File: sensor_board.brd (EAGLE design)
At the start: 24.9 x 49.9 mm, 9 parts, among them J1 2p-2.54, Q1 S8050

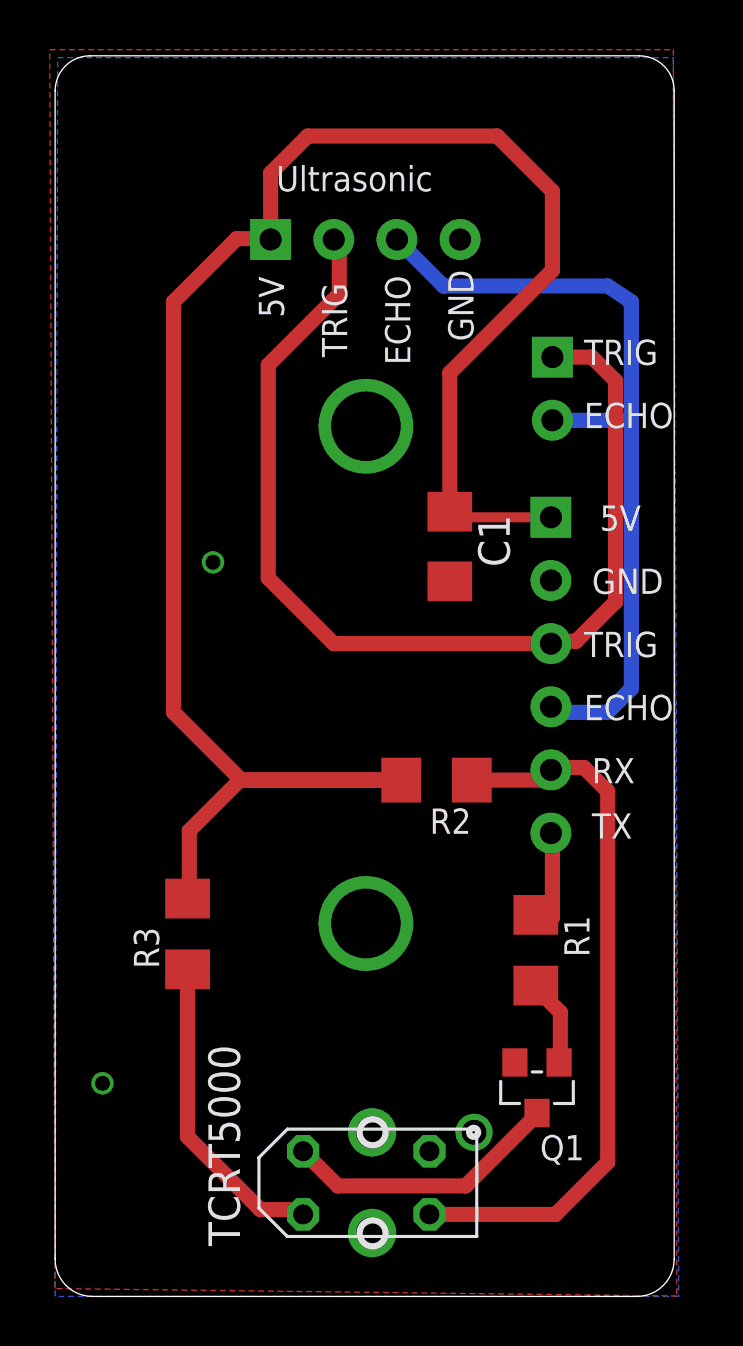
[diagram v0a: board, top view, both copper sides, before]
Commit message: PCB cosmetic changes
now, READY for sensing to SEEED for v1 fabrication.
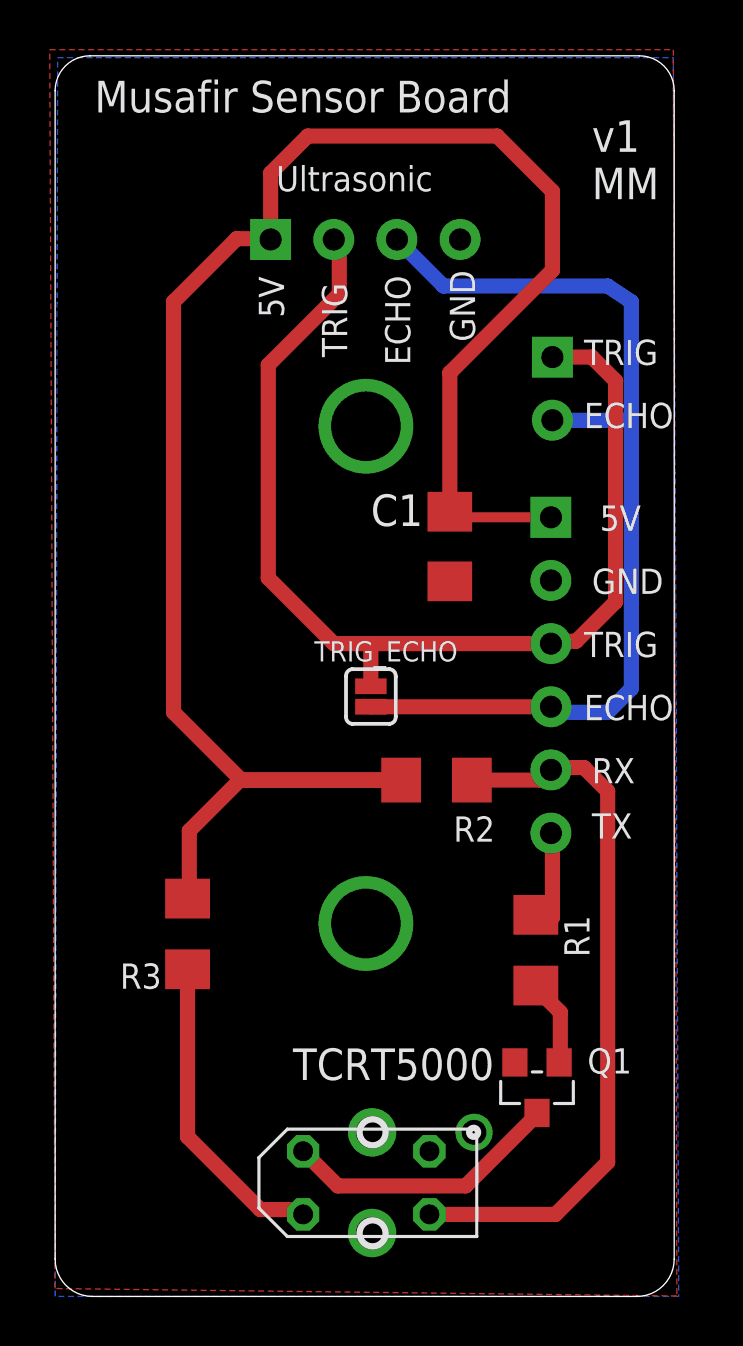
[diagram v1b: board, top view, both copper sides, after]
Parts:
- added TRIG_ECHO: (no value), SparkFun-Retired:SJ_2S
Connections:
- net ECHO: now also TRIG_ECHO.2
- net TRIG: now also TRIG_ECHO.1
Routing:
- net ECHO: track 33.5 -> 40.5 mm
- net TRIG: track 42.5 -> 44.2 mm
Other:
- board text added: "MM"
- board text added: "Musafir Sensor Board"
- board text added: "ejaadtech.com"
- board text added: "v1"
- board text removed: "EjadTech Ejadtech.com"
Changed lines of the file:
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@@
 <?xml version="1.0" encoding="utf-8"?>
 <!DOCTYPE eagle SYSTEM "eagle.dtd">
-<eagle version="7.6.0">
+<eagle version="7.2.0">
 <drawing>
 <settings>
@@
 <text x="11.7475" y="37.7825" size="1.016" layer="25" font="vector" ratio="12" rot="R90">TRIG</text>
 <text x="14.2875" y="37.465" size="1.016" layer="25" font="vector" ratio="12" rot="R90">ECHO</text>
-<text x="16.8275" y="38.4175" size="1.016" layer="25" font="vector" ratio="12" rot="R90">GND</text>
-<text x="18.415" y="30.7975" size="1.016" layer="26" font="vector" ratio="12" rot="MR0">5V</text>
-<text x="18.415" y="28.2575" size="1.016" layer="26" font="vector" ratio="12" rot="MR0">GND</text>
-<text x="18.7325" y="25.7175" size="1.016" layer="26" font="vector" ratio="12" rot="MR0">TRIG</text>
-<text x="18.615" y="23.1775" size="1.016" layer="26" font="vector" ratio="12" rot="MR0">ECHO</text>
-<text x="18.415" y="20.6375" size="1.016" layer="26" font="vector" ratio="12" rot="MR0">RX</text>
-<text x="18.415" y="18.0975" size="1.016" layer="26" font="vector" ratio="12" rot="MR0">TX</text>
+<text x="15.875" y="41.275" size="1.016" layer="25" font="vector" ratio="12" rot="R270">GND</text>
+<text x="17.78" y="30.7975" size="1.016" layer="26" font="vector" ratio="12" rot="MR0">5V</text>
+<text x="17.78" y="28.2575" size="1.016" layer="26" font="vector" ratio="12" rot="MR0">GND</text>
+<text x="18.0975" y="25.7175" size="1.016" layer="26" font="vector" ratio="12" rot="MR0">TRIG</text>
+<text x="17.98" y="23.1775" size="1.016" layer="26" font="vector" ratio="12" rot="MR0">ECHO</text>
+<text x="17.78" y="20.6375" size="1.016" layer="26" font="vector" ratio="12" rot="MR0">RX</text>
+<text x="17.78" y="18.0975" size="1.016" layer="26" font="vector" ratio="12" rot="MR0">TX</text>
 <text x="8.89" y="44.45" size="1.016" layer="25" font="vector" ratio="12">Ultrasonic</text>
-<text x="5.08" y="33.02" size="1.27" layer="26" font="vector" ratio="12" rot="MR270">EjadTech
-Ejadtech.com</text>
+<text x="5.3975" y="48.5775" size="1.27" layer="26" font="vector" ratio="12" rot="MR180">ejaadtech.com</text>
 <text x="21.2725" y="34.925" size="1.016" layer="25" font="vector" ratio="12">ECHO</text>
 <text x="21.2725" y="37.465" size="1.016" layer="25" font="vector" ratio="12">TRIG</text>
@@
 <text x="21.59" y="20.6375" size="1.016" layer="25" font="vector" ratio="12">RX</text>
 <text x="21.59" y="18.415" size="1.016" layer="25" font="vector" ratio="12">TX</text>
+<text x="1.5875" y="47.625" size="1.27" layer="25" font="vector" ratio="12" rot="SR0">Musafir Sensor Board</text>
+<text x="21.59" y="46.0375" size="1.27" layer="25" font="vector" ratio="12" rot="SR0">v1</text>
+<text x="21.59" y="44.1325" size="1.27" layer="25" font="vector" ratio="12" rot="SR0">MM</text>
 </plain>
 <attributes>
@@
 <element name="INPUT" library="Seeed-Connector -2016" package="H6-2.54" value="6p-2.54" x="19.9425" y="24.9875" smashed="yes" rot="MR0">
 <attribute name="MPN" value="F185-1106A1BSYC1" x="19.9425" y="24.9875" size="1.778" layer="28" rot="MR0" display="off"/>
-<attribute name="VALUE" x="17.4025" y="23.0825" size="0.889" layer="28" ratio="11" rot="MR90"/>
 <attribute name="NAME" x="21.53" y="24.035" size="1.016" layer="26" font="vector" ratio="12" rot="MR90"/>
 <attribute name="NAME" x="19.3075" y="22.4475" size="0.635" layer="34" ratio="10" rot="MR90"/>
@@
 <attribute name="MPN" value="F185-1104A1BSYA1" x="12.4775" y="42.5125" size="1.778" layer="28" rot="MR270" display="off"/>
 <attribute name="NAME" x="15.0175" y="44.735" size="1.016" layer="26" font="vector" ratio="12" rot="MR0"/>
-<attribute name="VALUE" x="14.3825" y="39.9725" size="0.889" layer="28" ratio="11" rot="MR0"/>
 </element>
 <element name="Q1" library="Seeed-Transistor-2016" package="SOT-23" value="S8050" x="19.3825" y="8.395" smashed="yes" rot="R180">
 <attribute name="MPN" value="S8050" x="19.3825" y="8.395" size="1.778" layer="27" rot="R180" display="off"/>
-<attribute name="NAME" x="21.2875" y="6.49" size="1.016" layer="25" font="vector" ratio="12" rot="R180"/>
-<attribute name="VALUE" x="20.6525" y="11.189" size="0.635" layer="27" ratio="10" rot="R180"/>
+<attribute name="NAME" x="23.1925" y="9.9825" size="1.016" layer="25" font="vector" ratio="12" rot="R180"/>
 </element>
 <element name="R1" library="adafruit" package="R1206" value="" x="19.335" y="13.925" smashed="yes" rot="R270">
@@
 </element>
 <element name="R2" library="adafruit" package="R1206" value="" x="15.34" y="20.7675" smashed="yes" rot="R180">
-<attribute name="NAME" x="16.737" y="19.6245" size="1.016" layer="25" font="vector" ratio="12" rot="R180"/>
+<attribute name="NAME" x="17.6895" y="19.307" size="1.016" layer="25" font="vector" ratio="12" rot="R180"/>
 <attribute name="VALUE" x="16.737" y="23.1805" size="1.27" layer="27" rot="R180"/>
 </element>
 <element name="R3" library="adafruit" package="R1206" value="" x="5.3275" y="14.58" smashed="yes" rot="R90">
-<attribute name="NAME" x="4.1845" y="13.183" size="1.016" layer="25" font="vector" ratio="12" rot="R90"/>
+<attribute name="NAME" x="4.2795" y="13.392" size="1.016" layer="25" font="vector" ratio="12" rot="R180"/>
 <attribute name="VALUE" x="7.7405" y="13.183" size="1.27" layer="27" rot="R90"/>
 </element>
 <element name="TCRT5000" library="tcrt5000" package="TCRT5000" value="" x="12.515" y="4.57" smashed="yes">
-<attribute name="NAME" x="7.435" y="2.03" size="1.27" layer="25" font="vector" ratio="12" rot="R90"/>
+<attribute name="NAME" x="17.655" y="9.975" size="1.27" layer="25" font="vector" ratio="12" rot="R180"/>
 <attribute name="VALUE" x="18.865" y="2.03" size="1.27" layer="21" rot="R90"/>
 </element>
 <element name="C1" library="adafruit" package="C1206" value="" x="15.875" y="30.1625" smashed="yes" rot="R270">
-<attribute name="NAME" x="17.018" y="31.4325" size="1.27" layer="25" rot="R270"/>
+<attribute name="NAME" x="12.7" y="30.988" size="1.27" layer="25" font="vector" ratio="12"/>
 <attribute name="VALUE" x="13.462" y="31.4325" size="1.27" layer="27" rot="R270"/>
 </element>
 <element name="J1" library="Seeed-Connector -2016" package="H2-2.54" value="2p-2.54" x="20.0025" y="36.5125" smashed="yes" rot="MR0">
 <attribute name="MPN" value="P125-1102A0BS116A1" x="20.0025" y="36.5125" size="1.778" layer="28" rot="MR0" display="off"/>
-<attribute name="VALUE" x="17.4625" y="33.9725" size="0.889" layer="28" ratio="11" rot="MR90"/>
+</element>
+<element name="TRIG_ECHO" library="SparkFun-Retired" package="SJ_2S" value="" x="12.7" y="24.13" smashed="yes" rot="R270">
+<attribute name="NAME" x="16.1898" y="26.3525" size="0.8128" layer="25" font="vector" ratio="12" rot="R180"/>
+<attribute name="VALUE" x="11.049" y="25.0798" size="0.4064" layer="27" rot="R270"/>
 </element>
 </elements>
@@
 <wire x1="11.43" y1="40.3225" x2="11.43" y2="42.29" width="0.6096" layer="1"/>
 <wire x1="11.43" y1="42.29" x2="11.2075" y2="42.5125" width="0.6096" layer="1"/>
-<wire x1="11.2075" y1="26.2575" x2="19.9425" y2="26.2575" width="0.6096" layer="1"/>
+<wire x1="11.2075" y1="26.2575" x2="12.7" y2="26.2575" width="0.6096" layer="1"/>
+<wire x1="12.7" y1="26.2575" x2="19.9425" y2="26.2575" width="0.6096" layer="1"/>
 <wire x1="20.0025" y1="37.7825" x2="21.59" y2="37.7825" width="0.6096" layer="1"/>
 <wire x1="22.5425" y1="27.94" x2="20.955" y2="26.3525" width="0.6096" layer="1"/>
@@
 <wire x1="22.5425" y1="27.94" x2="22.5425" y2="36.83" width="0.6096" layer="1"/>
 <wire x1="22.5425" y1="36.83" x2="21.59" y2="37.7825" width="0.6096" layer="1"/>
+<contactref element="TRIG_ECHO" pad="1"/>
+<wire x1="12.7" y1="24.5419" x2="12.7" y2="26.2575" width="0.6096" layer="1"/>
 </signal>
 <signal name="5V">
@@
 <contactref element="INPUT" pad="4"/>
 <contactref element="J1" pad="2"/>
-<wire x1="19.72" y1="23.495" x2="19.9425" y2="23.7175" width="0.6096" layer="1"/>
 <wire x1="13.7475" y1="42.5125" x2="13.7475" y2="42.1325" width="0.6096" layer="16"/>
 <wire x1="23.1775" y1="24.4475" x2="22.225" y2="23.495" width="0.6096" layer="16"/>
@@
 <wire x1="23.1775" y1="40.005" x2="23.1775" y2="35.2425" width="0.6096" layer="16"/>
 <wire x1="23.1775" y1="35.2425" x2="23.1775" y2="24.4475" width="0.6096" layer="16"/>
+<contactref element="TRIG_ECHO" pad="2"/>
+<wire x1="19.9425" y1="23.7175" x2="12.7" y2="23.7175" width="0.6096" layer="1"/>
+<wire x1="12.7" y1="23.7175" x2="12.7" y2="23.7181" width="0.6096" layer="1"/>
 </signal>
 <signal name="GND">
@@
 </polygon>
 <contactref element="C1" pad="2"/>
-<via x="6.35" y="29.5275" extent="1-16" drill="0.6" shape="square"/>
-<via x="1.905" y="8.5725" extent="1-16" drill="0.6" shape="square"/>
 </signal>
 <signal name="N$6">
@@
 </board>
 </drawing>
-<compatibility>
-<note version="6.3" minversion="6.2.2" severity="warning">
-Since Version 6.2.2 text objects can contain more than one line,
-which will not be processed correctly with this version.
-</note>
-</compatibility>
 </eagle>
